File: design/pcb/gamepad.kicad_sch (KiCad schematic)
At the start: 17 parts, among them J1 B2B-XH-A, J10 B2B-XH-A, J11 B2B-XH-A, J12 B2B-XH-A, J13 B2B-XH-A, J14 B2B-XH-A, J15 B2B-XH-A, J16 B2B-XH-A, J2 B2B-XH-A, J3 B2B-XH-A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

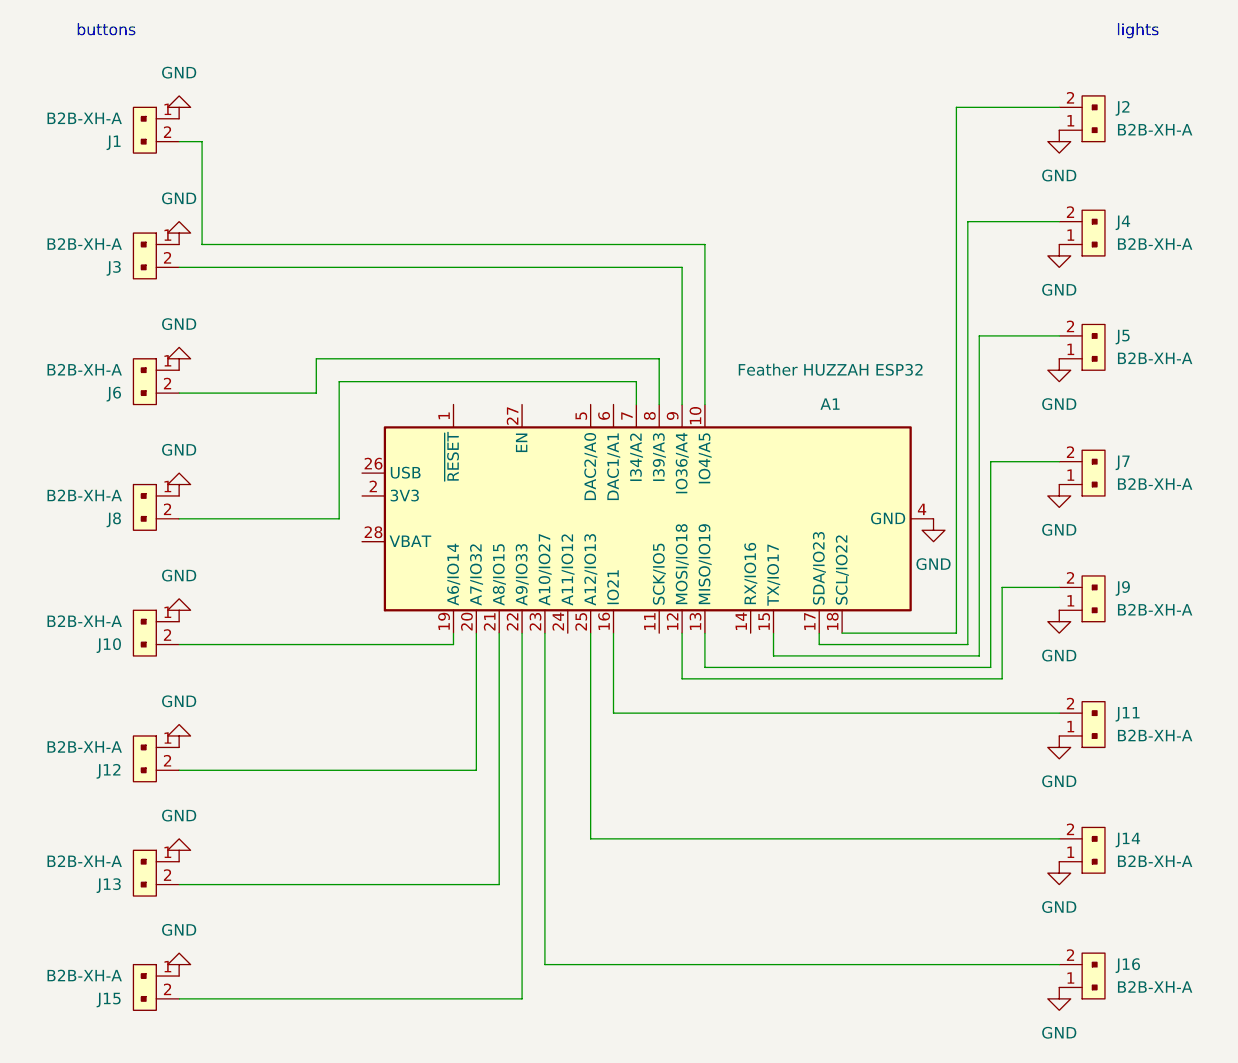
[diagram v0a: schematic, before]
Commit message: firmware update, fix an oopsie in the pcb
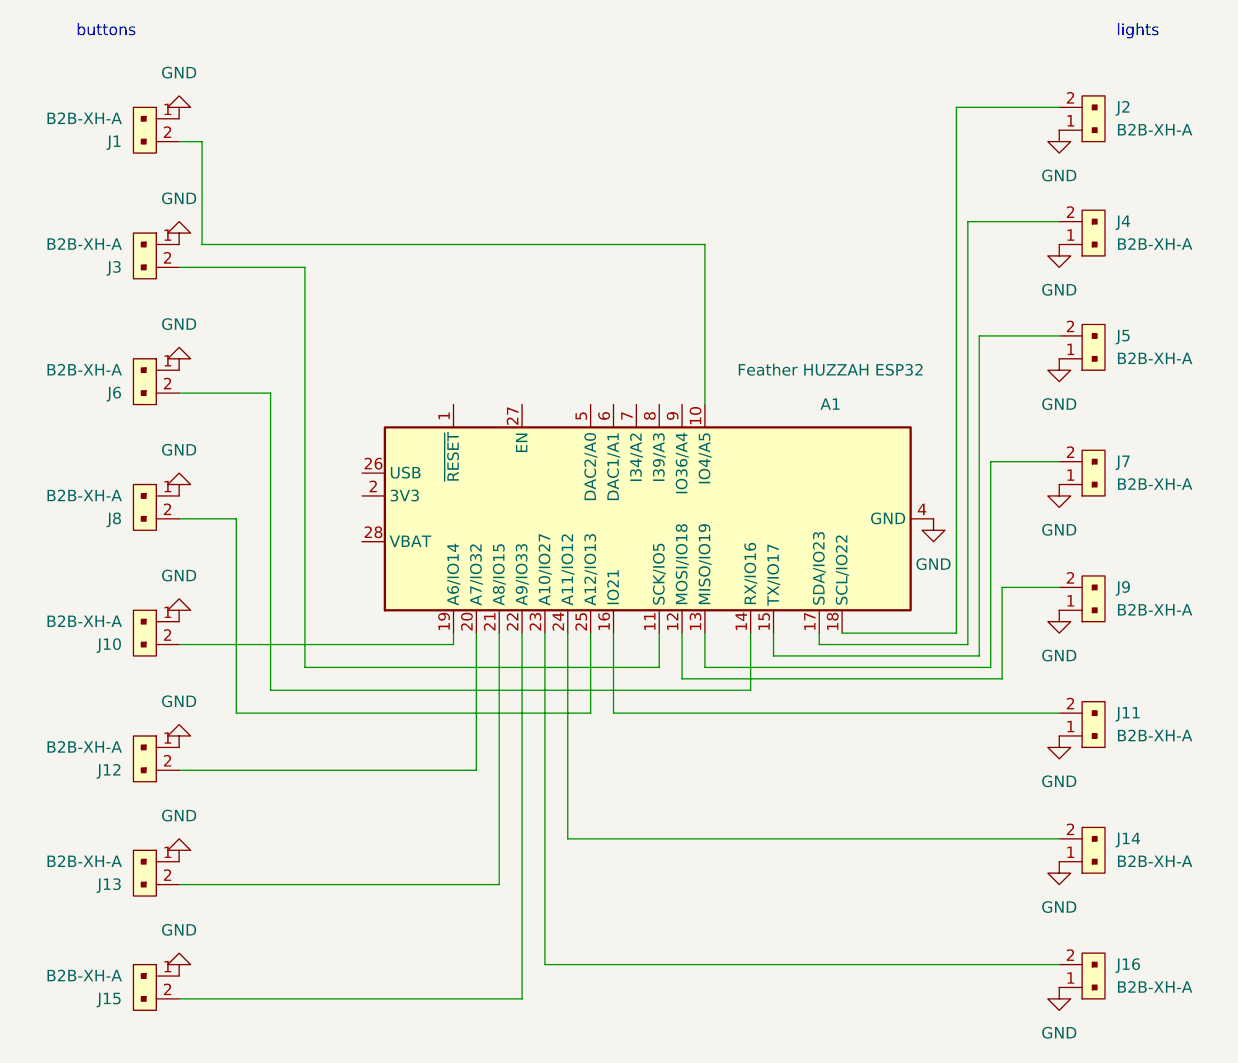
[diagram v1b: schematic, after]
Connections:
- net at J6.2: now also A1.14 (RX/IO16); no longer A1.8 (I39/A3)
- net at J3.2: now also A1.11 (SCK/IO5); no longer A1.9 (IO36/A4)
- net at A1.24 (A11/IO12): now also J14.2
- net at A1.25 (A12/IO13): now also J8.2; no longer J14.2
- net at A1.7 (I34/A2): no longer J8.2
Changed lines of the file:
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@@
-    (stroke (width 0) (type default) (color 0 0 0 0))
-  )
-  (wire (pts (xy 72.39 59.69) (xy 110.49 59.69))
-    (stroke (width 0) (type default) (color 0 0 0 0))
-  )
-  (wire (pts (xy 113.03 49.53) (xy 113.03 64.77))
     (stroke (width 0) (type default) (color 0 0 0 0))
   )
@@
     (stroke (width 0) (type default) (color 0 0 0 0))
   )
-  (wire (pts (xy 57.15 63.5) (xy 72.39 63.5))
+  (wire (pts (xy 57.15 49.53) (xy 71.12 49.53))
     (stroke (width 0) (type default) (color 0 0 0 0))
   )
@@
     (stroke (width 0) (type default) (color 0 0 0 0))
   )
-  (wire (pts (xy 74.93 62.23) (xy 107.95 62.23))
+  (wire (pts (xy 71.12 49.53) (xy 71.12 93.98))
     (stroke (width 0) (type default) (color 0 0 0 0))
   )
@@
     (stroke (width 0) (type default) (color 0 0 0 0))
   )
-  (wire (pts (xy 107.95 62.23) (xy 107.95 64.77))
+  (wire (pts (xy 71.12 93.98) (xy 110.49 93.98))
+    (stroke (width 0) (type default) (color 0 0 0 0))
+  )
+  (wire (pts (xy 102.87 99.06) (xy 102.87 90.17))
+    (stroke (width 0) (type default) (color 0 0 0 0))
+  )
+  (wire (pts (xy 63.5 99.06) (xy 102.87 99.06))
+    (stroke (width 0) (type default) (color 0 0 0 0))
+  )
+  (wire (pts (xy 63.5 77.47) (xy 63.5 99.06))
     (stroke (width 0) (type default) (color 0 0 0 0))
   )
   (wire (pts (xy 146.05 92.71) (xy 123.19 92.71))
+    (stroke (width 0) (type default) (color 0 0 0 0))
+  )
+  (wire (pts (xy 67.31 63.5) (xy 67.31 96.52))
     (stroke (width 0) (type default) (color 0 0 0 0))
   )
@@
     (stroke (width 0) (type default) (color 0 0 0 0))
   )
-  (wire (pts (xy 57.15 118.11) (xy 92.71 118.11))
+  (wire (pts (xy 67.31 96.52) (xy 120.65 96.52))
     (stroke (width 0) (type default) (color 0 0 0 0))
   )
-  (wire (pts (xy 57.15 49.53) (xy 113.03 49.53))
+  (wire (pts (xy 57.15 118.11) (xy 92.71 118.11))
     (stroke (width 0) (type default) (color 0 0 0 0))
   )
@@
   )
   (wire (pts (xy 154.94 127) (xy 97.79 127))
-    (stroke (width 0) (type default) (color 0 0 0 0))
-  )
-  (wire (pts (xy 102.87 113.03) (xy 102.87 90.17))
     (stroke (width 0) (type default) (color 0 0 0 0))
   )
@@
     (stroke (width 0) (type default) (color 0 0 0 0))
   )
-  (wire (pts (xy 110.49 59.69) (xy 110.49 64.77))
+  (wire (pts (xy 154.94 71.12) (xy 147.32 71.12))
     (stroke (width 0) (type default) (color 0 0 0 0))
   )
-  (wire (pts (xy 154.94 71.12) (xy 147.32 71.12))
+  (wire (pts (xy 57.15 77.47) (xy 63.5 77.47))
+    (stroke (width 0) (type default) (color 0 0 0 0))
+  )
+  (wire (pts (xy 57.15 63.5) (xy 67.31 63.5))
+    (stroke (width 0) (type default) (color 0 0 0 0))
+  )
+  (wire (pts (xy 100.33 113.03) (xy 100.33 90.17))
     (stroke (width 0) (type default) (color 0 0 0 0))
   )
@@
     (stroke (width 0) (type default) (color 0 0 0 0))
   )
-  (wire (pts (xy 72.39 63.5) (xy 72.39 59.69))
+  (wire (pts (xy 110.49 93.98) (xy 110.49 90.17))
     (stroke (width 0) (type default) (color 0 0 0 0))
   )
   (wire (pts (xy 154.94 44.45) (xy 144.78 44.45))
+    (stroke (width 0) (type default) (color 0 0 0 0))
+  )
+  (wire (pts (xy 120.65 96.52) (xy 120.65 90.17))
     (stroke (width 0) (type default) (color 0 0 0 0))
   )
@@
   )
   (wire (pts (xy 147.32 93.98) (xy 115.57 93.98))
-    (stroke (width 0) (type default) (color 0 0 0 0))
-  )
-  (wire (pts (xy 74.93 77.47) (xy 74.93 62.23))
-    (stroke (width 0) (type default) (color 0 0 0 0))
-  )
-  (wire (pts (xy 57.15 77.47) (xy 74.93 77.47))
     (stroke (width 0) (type default) (color 0 0 0 0))
   )
@@
     (stroke (width 0) (type default) (color 0 0 0 0))
   )
-  (wire (pts (xy 154.94 113.03) (xy 102.87 113.03))
+  (wire (pts (xy 100.33 113.03) (xy 154.94 113.03))
     (stroke (width 0) (type default) (color 0 0 0 0))
   )
